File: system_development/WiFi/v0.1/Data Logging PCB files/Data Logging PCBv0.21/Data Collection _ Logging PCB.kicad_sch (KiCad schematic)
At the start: 7 parts, among them U1 TC2014-3.3VxCTTR

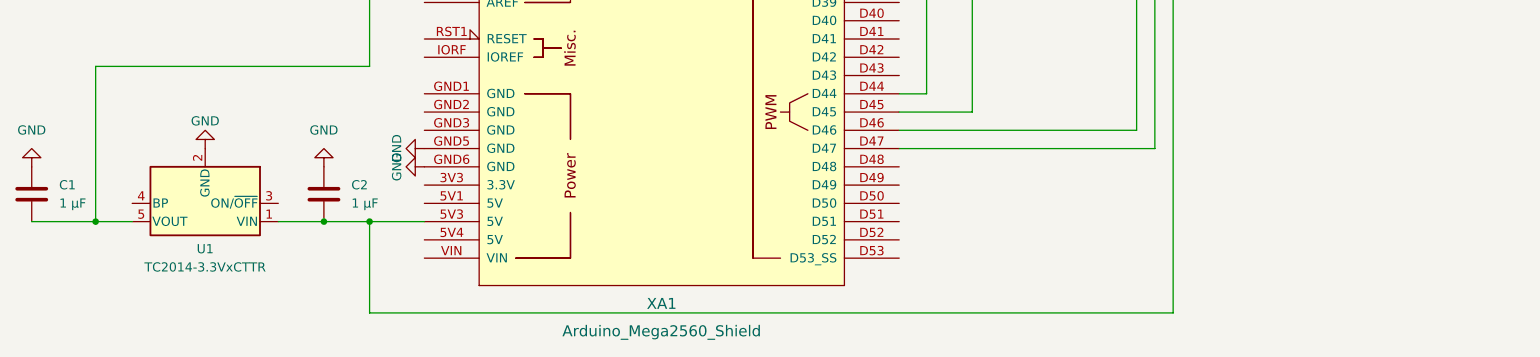
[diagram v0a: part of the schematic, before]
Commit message: Updated Wifi Code
Updated Wifi code to reflect some of the changes made to the cellular code, order of operations, failsafes.
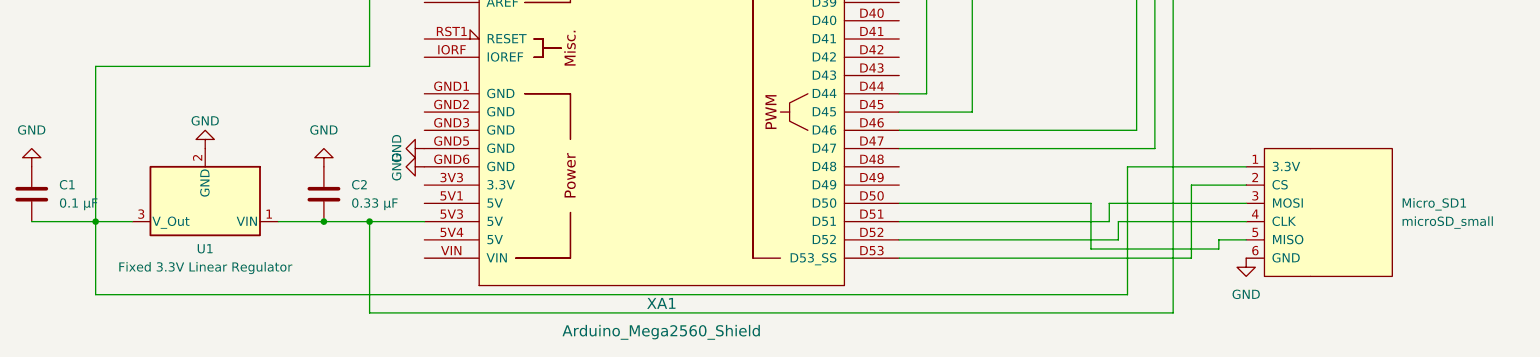
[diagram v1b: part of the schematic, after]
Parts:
- added Micro_SD1: microSD_small, Connector_PinSocket_2.54mm:PinSocket_1x06_P2.54mm_Vertical, symbol ARTS-Lab:microSD_small
- C1: value 1 µF -> 0.1 µF
- C2: value 1 µF -> 0.33 µF
- U1: value TC2014-3.3VxCTTR -> Fixed 3.3V Linear Regulator; footprint Package_TO_SOT_SMD:SOT-23-5 -> Package_TO_SOT_SMD:TO-252-3_TabPin2
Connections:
- net GND: now also Micro_SD1.6 (GND)
- net at C1.2, RT1.5 (VCC): now also U1.3 (V_Out), Micro_SD1.1 (3.3V); no longer U1.5 (VOUT)
- net at XA1.D50: now also Micro_SD1.5 (MISO)
- net at XA1.D51: now also Micro_SD1.3 (MOSI)
- net at XA1.D52: now also Micro_SD1.4 (CLK)
- net at XA1.D53 (D53_SS): now also Micro_SD1.2 (CS)
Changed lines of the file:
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@@
+    (stroke (width 0) (type default))
+  )
+  (wire (pts (xy 196.85 142.24) (xy 196.85 148.59))
     (stroke (width 0) (type default))
   )
@@
     (stroke (width 0) (type default))
   )
+  (wire (pts (xy 170.18 147.32) (xy 200.66 147.32))
+    (stroke (width 0) (type default))
+  )
   (wire (pts (xy 203.2 132.08) (xy 170.18 132.08))
     (stroke (width 0) (type default))
@@
     (stroke (width 0) (type default))
   )
+  (wire (pts (xy 199.39 142.24) (xy 218.44 142.24))
+    (stroke (width 0) (type default))
+  )
   (wire (pts (xy 227.33 99.06) (xy 203.2 99.06))
     (stroke (width 0) (type default))
   )
+  (wire (pts (xy 214.63 148.59) (xy 214.63 147.32))
+    (stroke (width 0) (type default))
+  )
   (wire (pts (xy 213.36 95.25) (xy 218.44 95.25))
     (stroke (width 0) (type default))
@@
     (stroke (width 0) (type default))
   )
+  (wire (pts (xy 196.85 148.59) (xy 214.63 148.59))
+    (stroke (width 0) (type default))
+  )
+  (wire (pts (xy 214.63 147.32) (xy 218.44 147.32))
+    (stroke (width 0) (type default))
+  )
+  (wire (pts (xy 170.18 149.86) (xy 210.82 149.86))
+    (stroke (width 0) (type default))
+  )
   (wire (pts (xy 72.39 78.74) (xy 72.39 82.55))
     (stroke (width 0) (type default))
   )
+  (wire (pts (xy 210.82 149.86) (xy 210.82 139.7))
+    (stroke (width 0) (type default))
+  )
   (wire (pts (xy 205.74 102.87) (xy 205.74 134.62))
     (stroke (width 0) (type default))
@@
     (stroke (width 0) (type default))
   )
+  (wire (pts (xy 201.93 154.94) (xy 58.42 154.94))
+    (stroke (width 0) (type default))
+  )
   (wire (pts (xy 208.28 106.68) (xy 227.33 106.68))
     (stroke (width 0) (type default))
@@
     (stroke (width 0) (type default))
   )
+  (wire (pts (xy 170.18 142.24) (xy 196.85 142.24))
+    (stroke (width 0) (type default))
+  )
+  (wire (pts (xy 170.18 144.78) (xy 199.39 144.78))
+    (stroke (width 0) (type default))
+  )
   (wire (pts (xy 208.28 157.48) (xy 208.28 106.68))
     (stroke (width 0) (type default))
@@
     (stroke (width 0) (type default))
   )
+  (wire (pts (xy 199.39 144.78) (xy 199.39 142.24))
+    (stroke (width 0) (type default))
+  )
   (wire (pts (xy 218.44 95.25) (xy 227.33 95.25))
     (stroke (width 0) (type default))
@@
     (stroke (width 0) (type default))
   )
+  (wire (pts (xy 210.82 139.7) (xy 218.44 139.7))
+    (stroke (width 0) (type default))
+  )
+  (wire (pts (xy 218.44 137.16) (xy 201.93 137.16))
+    (stroke (width 0) (type default))
+  )
   (wire (pts (xy 96.52 157.48) (xy 208.28 157.48))
     (stroke (width 0) (type default))
   )
+  (wire (pts (xy 58.42 144.78) (xy 58.42 154.94))
+    (stroke (width 0) (type default))
+  )
   (wire (pts (xy 49.53 144.78) (xy 58.42 144.78))
     (stroke (width 0) (type default))
@@
     (stroke (width 0) (type default))
   )
+  (wire (pts (xy 200.66 147.32) (xy 200.66 144.78))
+    (stroke (width 0) (type default))
+  )
   (wire (pts (xy 227.33 80.01) (xy 173.99 80.01))
+    (stroke (width 0) (type default))
+  )
+  (wire (pts (xy 201.93 137.16) (xy 201.93 154.94))
+    (stroke (width 0) (type default))
+  )
+  (wire (pts (xy 200.66 144.78) (xy 218.44 144.78))
     (stroke (width 0) (type default))
   )
@@
   (symbol (lib_id "Device:C") (at 49.53 140.97 0) (unit 1)
     (in_bom yes) (on_board yes) (dnp no) (fields_autoplaced)
-    (property "Reference" "C1" (at 53.34 139.6999 0)
-      (effects (font (size 1.27 1.27)) (justify left))
-    )
-    (property "Value" "1 µF" (at 53.34 142.2399 0)
+    (property "Reference" "C1" (at 53.34 139.7 0)
+      (effects (font (size 1.27 1.27)) (justify left))
+    )
+    (property "Value" "0.1 µF" (at 53.34 142.24 0)
       (effects (font (size 1.27 1.27)) (justify left))
     )
@@
       (effects (font (size 1.27 1.27)) hide)
     )
-    (property "Datasheet" "https://mm.digikey.com/Volume0/opasdata/d220001/medias/docus/503/CL31B105KBHNNNE_Char.pdf" (at 49.53 140.97 0)
+    (property "Datasheet" "https://mm.digikey.com/Volume0/opasdata/d220001/medias/docus/1256/CL31B104KBCNNNC_Spec.pdf" (at 49.53 140.97 0)
       (effects (font (size 1.27 1.27)) hide)
     )
@@
         (path "/0fbf51aa-9f7e-4b3e-beb6-3112974e4ac2"
           (reference "#PWR02") (unit 1)
+        )
+      )
+    )
+  )
+  (symbol (lib_id "power:GND") (at 218.44 149.86 0) (unit 1)
+    (in_bom yes) (on_board yes) (dnp no) (fields_autoplaced)
+    (property "Reference" "#PWR010" (at 218.44 156.21 0)
+      (effects (font (size 1.27 1.27)) hide)
+    )
+    (property "Value" "GND" (at 218.44 154.94 0)
+      (effects (font (size 1.27 1.27)))
+    )
+    (property "Footprint" "" (at 218.44 149.86 0)
+      (effects (font (size 1.27 1.27)) hide)
+    )
+    (property "Datasheet" "" (at 218.44 149.86 0)
+      (effects (font (size 1.27 1.27)) hide)
+    )
+    (pin "1")
+    (instances
+      (project "Data Collection _ Logging PCB"
+        (path "/0fbf51aa-9f7e-4b3e-beb6-3112974e4ac2"
+          (reference "#PWR010") (unit 1)
         )
       )
@@
   (symbol (lib_id "Device:C") (at 90.17 140.97 0) (unit 1)
     (in_bom yes) (on_board yes) (dnp no) (fields_autoplaced)
-    (property "Reference" "C2" (at 93.98 139.6999 0)
-      (effects (font (size 1.27 1.27)) (justify left))
-    )
-    (property "Value" "1 µF" (at 93.98 142.2399 0)
+    (property "Reference" "C2" (at 93.98 139.7 0)
+      (effects (font (size 1.27 1.27)) (justify left))
+    )
+    (property "Value" "0.33 µF" (at 93.98 142.24 0)
       (effects (font (size 1.27 1.27)) (justify left))
     )
@@
       (effects (font (size 1.27 1.27)) hide)
     )
-    (property "Datasheet" "https://mm.digikey.com/Volume0/opasdata/d220001/medias/docus/503/CL31B105KBHNNNE_Char.pdf" (at 90.17 140.97 0)
+    (property "Datasheet" "https://www.samsungsem.com/resources/file/global/support/product_catalog/MLCC.pdf" (at 90.17 140.97 0)
       (effects (font (size 1.27 1.27)) hide)
     )
@@
       (effects (font (size 1.27 1.27)))
     )
-    (property "Value" "TC2014-3.3VxCTTR" (at 73.66 151.13 0)
-      (effects (font (size 1.27 1.27)))
-    )
-    (property "Footprint" "Package_TO_SOT_SMD:SOT-23-5" (at 73.66 150.495 0)
-      (effects (font (size 1.27 1.27)) hide)
-    )
-    (property "Datasheet" "http://ww1.microchip.com/downloads/en/DeviceDoc/21662F.pdf" (at 73.66 142.24 0)
+    (property "Value" "Fixed 3.3V Linear Regulator" (at 73.66 151.13 0)
+      (effects (font (size 1.27 1.27)))
+    )
+    (property "Footprint" "Package_TO_SOT_SMD:TO-252-3_TabPin2" (at 73.66 150.495 0)
+      (effects (font (size 1.27 1.27)) hide)
+    )
+    (property "Datasheet" "https://www.ti.com/lit/ds/slvs059u/slvs059u.pdf?ts=1720791929813" (at 73.66 142.24 0)
       (effects (font (size 1.27 1.27)) hide)
     )
@@
     (pin "2")
     (pin "3")
-    (pin "4")
-    (pin "5")
     (instances
       (project "Data Collection _ Logging PCB"
@@
         )
       )
+    )
+  )
+  (symbol (lib_id "ARTS-Lab:microSD_small") (at 238.76 143.51 270) (unit 1)
+    (in_bom yes) (on_board yes) (dnp no) (fields_autoplaced)
+    (property "Reference" "Micro_SD1" (at 240.03 142.2399 90)
+      (effects (font (size 1.27 1.27)) (justify left))
+    )
+    (property "Value" "microSD_small" (at 240.03 144.7799 90)
+      (effects (font (size 1.27 1.27)) (justify left))
+    )
+    (property "Footprint" "Connector_PinSocket_2.54mm:PinSocket_1x06_P2.54mm_Vertical" (at 238.76 143.51 0)
+      (effects (font (size 1.27 1.27)) hide)
+    )
+    (property "Datasheet" "" (at 238.76 143.51 0)
+      (effects (font (size 1.27 1.27)) hide)
+    )
+    (pin "1")
+    (pin "2")
+    (pin "3")
+    (pin "4")
+    (pin "5")
+    (pin "6")
+    (instances
+      (project "Data Collection _ Logging PCB"
+        (path "/0fbf51aa-9f7e-4b3e-beb6-3112974e4ac2"
+          (reference "Micro_SD1") (unit 1)
+        )
+      )
